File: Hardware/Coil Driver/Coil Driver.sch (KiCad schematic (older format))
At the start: 76 parts, among them J1 Barrel_Jack_Switch, J2 0.1\" Header, J3 Tag-connect-NL, J4 0.1\" Header, Q1 DMN3023L, Q2 DMN3023L, Q3 DMN3023L, Q4 DMN3023L, SW1 BTN_RST, SW2 BTN_USR1, SW3 BTN_USR2, U1 DGD05473, U2 MCP16331, U3 DGD05473, U4 STM32F070F6P6, Y1 8MHz

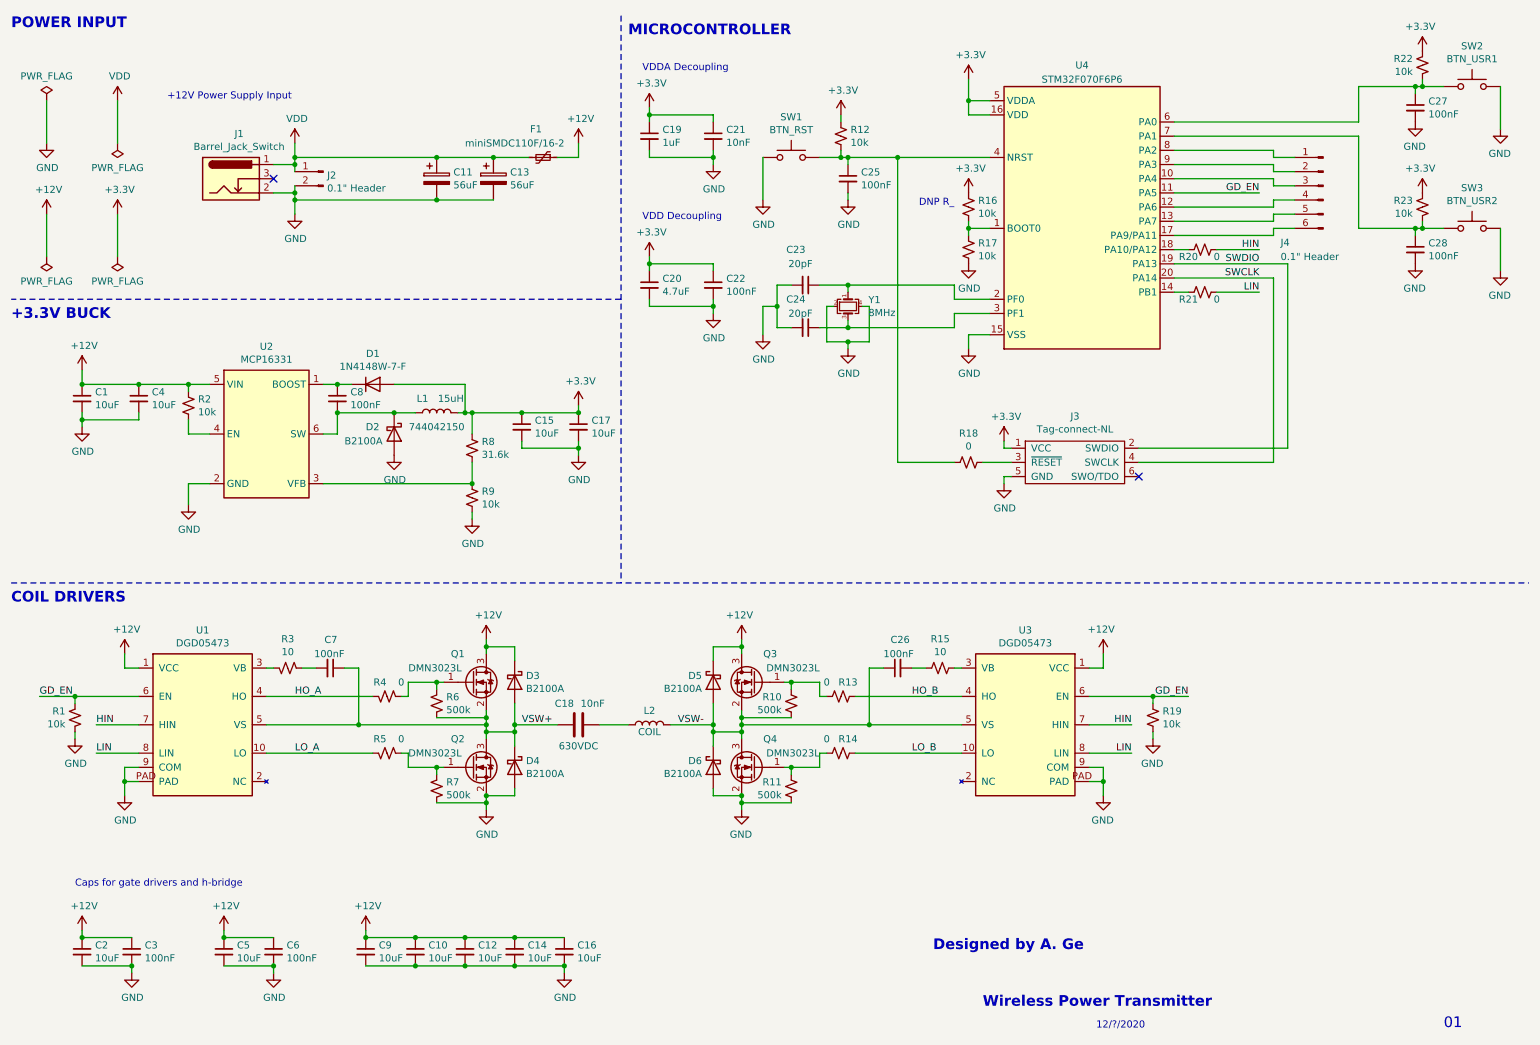
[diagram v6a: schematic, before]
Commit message: imported footprints into PCB document. Added user LEDs and power indication LEDs to schematic.
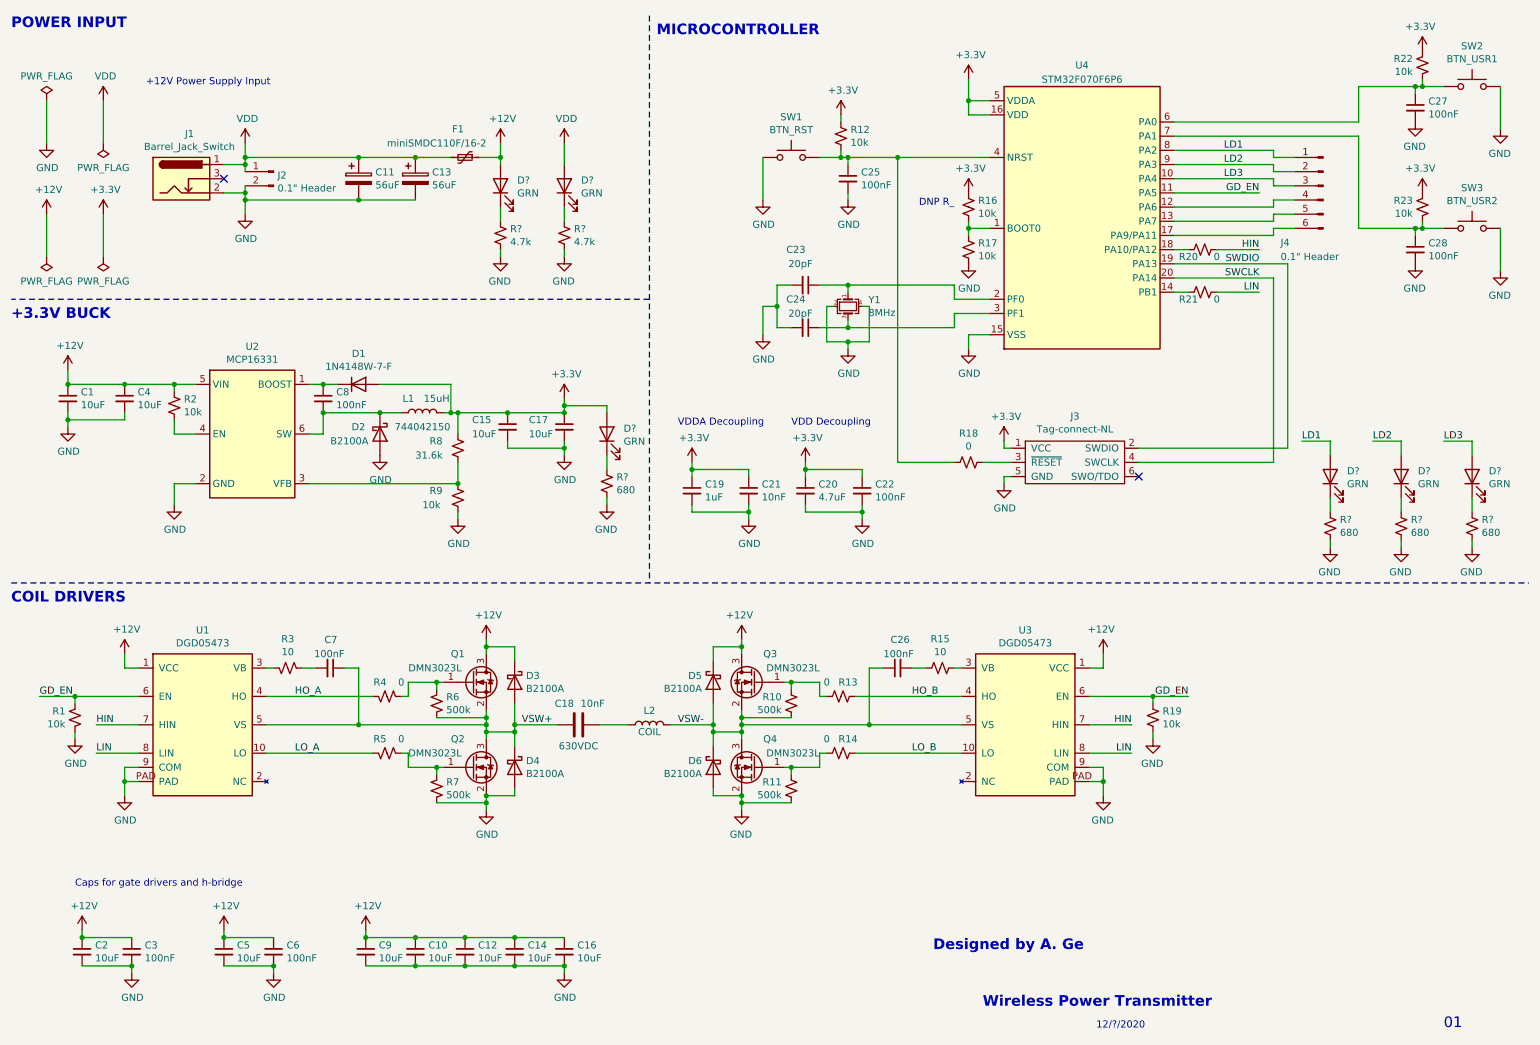
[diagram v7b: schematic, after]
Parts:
- added D? (x6): GRN, symbol Device:LED
- added R? (x4): 680, symbol Device:R_Small_US
- added R? (x2): 4.7k, symbol Device:R_Small_US
- C18: footprint Capacitor_THT:C_Rect_L7.2mm_W8.5mm_P5.00mm_FKS2_FKP2_MKS2_MKP2 -> Capacitor_THT:C_Rect_L7.2mm_W8.5mm_P5.00mm_FKP2_FKP2_MKS2_MKP2
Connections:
- net +12V: now also D?.2 (A)
- net +3V3: now also D?.2 (A)
- net GND: now also R?.2, R?.2, R?.2, R?.2, R?.2, R?.2
- net VDD: now also D?.2 (A)
- net LD3: now reaches J4.3 (Pin_3), U4.10 (PA4)
- net LD3: now also D?.2 (A)
- net LD1: now reaches J4.1 (Pin_1), U4.8 (PA2)
- net LD1: now also D?.2 (A)
- net LD2: now reaches J4.2 (Pin_2), U4.9 (PA3)
- net LD2: now also D?.2 (A)
- new net: D?.1 (K), R?.1 (x6)
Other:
- moved on the sheet: C1, C11, C13, C15, C17, C19, C20, C21, C22, C4, C8, D1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

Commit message: Swapped out 8MHz crystal for 2 pin instead of 4 pin. Initial part placement (except for gate drivers/h-bridge) loosely complete. Decided board will be 4 layers to make routing of power nets easier.
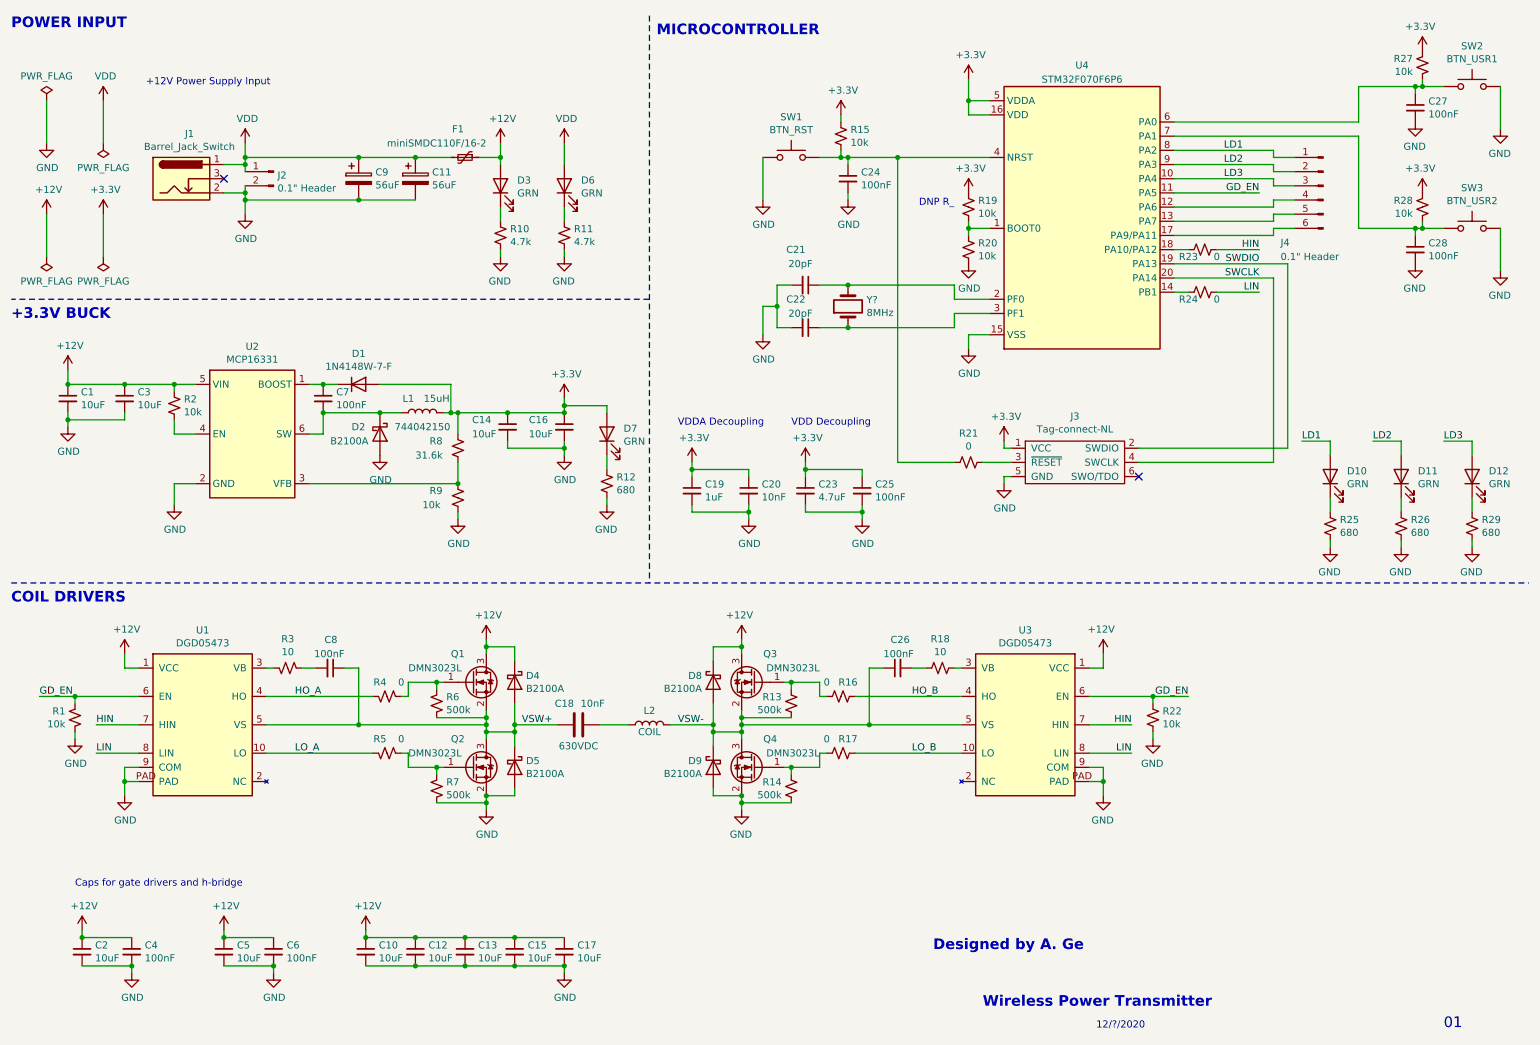
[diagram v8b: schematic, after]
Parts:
- removed Y1: 8MHz, Crystal:Crystal_SMD_5032-4Pin_5.0x3.2mm, symbol Device:Crystal_GND24_Small
- added Y?: 8MHz, symbol Device:Crystal
- D10, D11, D12, D3, D6, D7: renamed from D?; footprint (none) -> LED_SMD:LED_0603_1608Metric
- R10, R11, R12, R25, R26, R29: renamed from R?; footprint (none) -> Resistor_SMD:R_0603_1608Metric
- renumbered C9 to C10, C13 to C11, C10 to C12, C12 to C13, C15 to C14, C14 to C15, C17 to C16, C16 to C17, C21 to C20, C23 to C21, C24 to C22, C20 to C23, C25 to C24, C22 to C25, C4 to C3, C3 to C4, C8 to C7, C7 to C8, C11 to C9, D3 to D4, D4 to D5, D5 to D8, D6 to D9, R10 to R13, R11 to R14, R12 to R15, R13 to R16, R14 to R17, R15 to R18, R16 to R19, R17 to R20, R18 to R21, R19 to R22, R20 to R23, R21 to R24, R22 to R27, R23 to R28
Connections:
- net at C21.1, U4.2 (PF0): now also Y?.2
- net at C22.1, U4.3 (PF1): now also Y?.1
